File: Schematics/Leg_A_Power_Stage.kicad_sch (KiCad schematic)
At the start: 40 parts, among them Q2 C3M0025065K, Q3 C3M0025065K, U1 UCC21710QDWRQ1, U2 UCC21710QDWRQ1

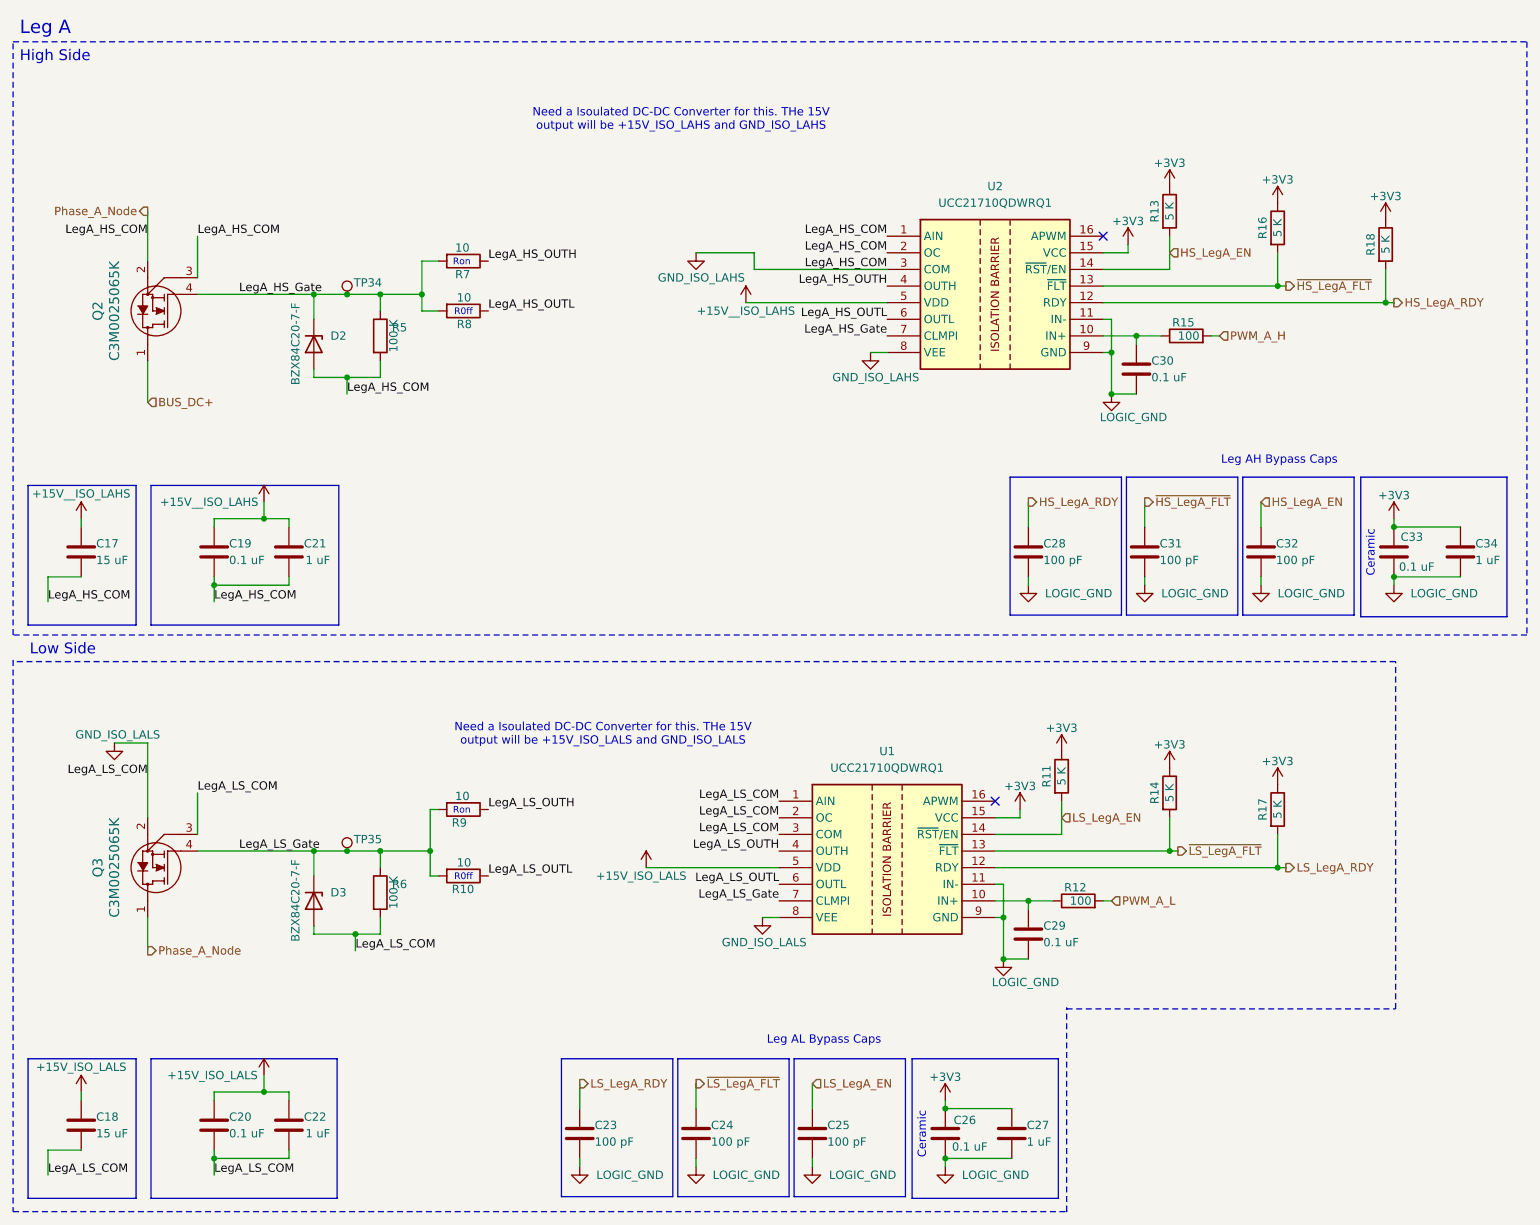
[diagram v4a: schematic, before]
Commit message: Fixing Full Bridge MOSFET ISO_GND to reference GND or DC-
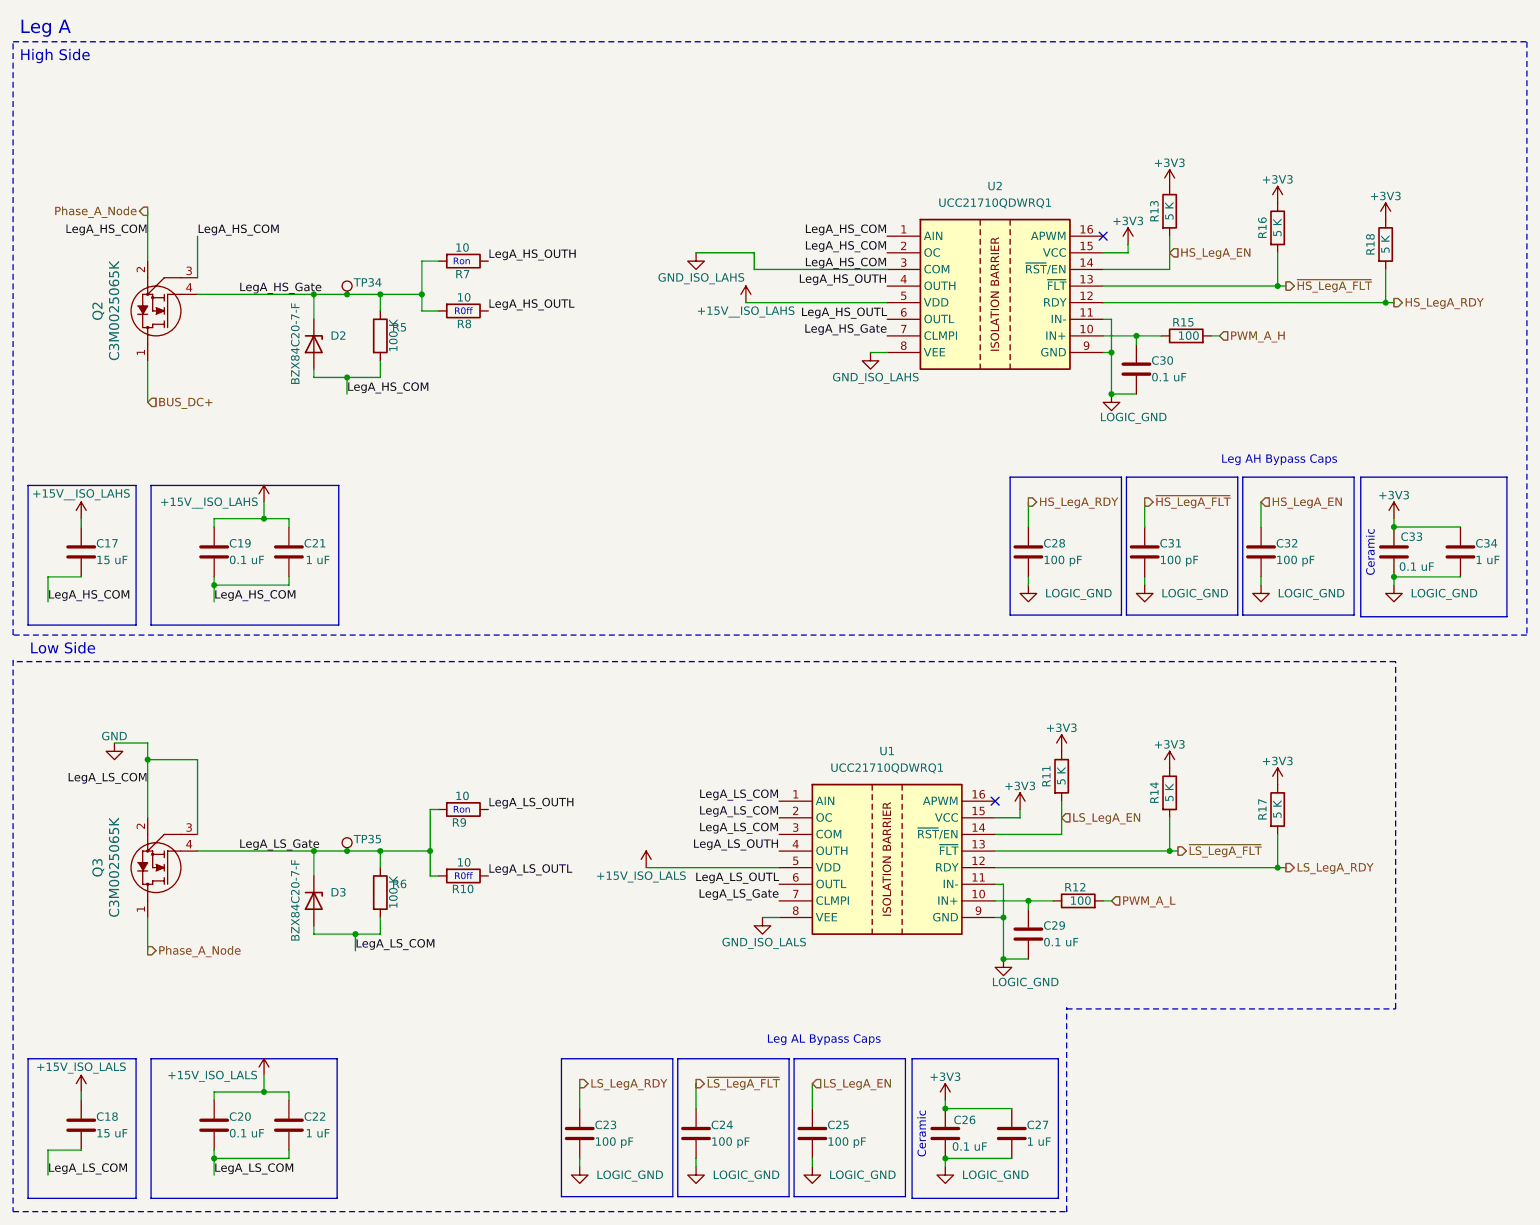
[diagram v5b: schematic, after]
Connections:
- net GND_ISO_LALS: no longer C18.2, C20.2, C22.2, D3.2 (A), Q3.2, Q3.3, R6.2, U1.1 (AIN), U1.2 (OC), U1.3 (COM)
- new net GND: C18.2, C20.2, C22.2, D3.2 (A), Q3.2, Q3.3, R6.2, U1.1 (AIN), U1.2 (OC), U1.3 (COM)
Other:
- note removed: "Need a Isoulated DC-DC Converter for this. THe 15V output will be +15V_ISO_LAHS and GND_ISO_LAHS"
- note removed: "Need a Isoulated DC-DC Converter for this. THe 15V output will be +15V_ISO_LALS and GND_ISO_LALS"
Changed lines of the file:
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@@
 		)
 	)
-	(text "Need a Isoulated DC-DC Converter for this. THe 15V\noutput will be +15V_ISO_LALS and GND_ISO_LALS"
-		(exclude_from_sim no)
-		(at 105.156 123.19 0)
-		(effects
-			(font
-				(size 1.27 1.27)
-			)
-		)
-	)
 	(text "Low Side\n"
 		(exclude_from_sim no)
@@
 		)
 	)
-	(text "Need a Isoulated DC-DC Converter for this. THe 15V\noutput will be +15V_ISO_LAHS and GND_ISO_LAHS"
-		(exclude_from_sim no)
-		(at 117.094 29.21 0)
-		(effects
-			(font
-				(size 1.27 1.27)
-			)
-		)
-	)
 	(text "Ceramic\n"
 		(exclude_from_sim no)
@@
 	)
 	(junction
+		(at 35.56 127)
+		(diameter 0)
+		(color 0 0 0 0)
+	)
+	(junction
 		(at 60.96 55.88)
 		(diameter 0)
@@
 	(wire
 		(pts
-			(xy 35.56 124.46) (xy 35.56 135.89)
+			(xy 168.91 134.62) (xy 168.91 135.89)
 		)
 		(stroke
@@
 	(wire
 		(pts
-			(xy 168.91 134.62) (xy 168.91 135.89)
+			(xy 45.72 187.96) (xy 45.72 190.5)
 		)
 		(stroke
@@
 	(wire
 		(pts
-			(xy 45.72 187.96) (xy 45.72 190.5)
+			(xy 119.38 187.96) (xy 119.38 189.23)
 		)
 		(stroke
@@
 	(wire
 		(pts
-			(xy 119.38 187.96) (xy 119.38 189.23)
+			(xy 170.18 148.59) (xy 173.99 148.59)
 		)
 		(stroke
@@
 	(wire
 		(pts
-			(xy 170.18 148.59) (xy 173.99 148.59)
+			(xy 208.28 138.43) (xy 208.28 143.51)
 		)
 		(stroke
@@
 	(wire
 		(pts
-			(xy 208.28 138.43) (xy 208.28 143.51)
+			(xy 43.18 127) (xy 35.56 127)
 		)
 		(stroke
@@
 	(wire
 		(pts
+			(xy 35.56 127) (xy 35.56 135.89)
+		)
+		(stroke
+			(width 0)
+			(type default)
+		)
+	)
+	(wire
+		(pts
 			(xy 71.12 140.97) (xy 71.12 143.51)
 		)
@@
 	(wire
 		(pts
-			(xy 43.18 132.08) (xy 43.18 138.43)
-		)
-		(stroke
-			(width 0)
-			(type default)
-		)
-	)
-	(wire
-		(pts
 			(xy 182.88 71.12) (xy 186.69 71.12)
 		)
@@
 	(wire
 		(pts
+			(xy 43.18 138.43) (xy 43.18 127)
+		)
+		(stroke
+			(width 0)
+			(type default)
+		)
+	)
+	(wire
+		(pts
 			(xy 45.72 99.06) (xy 45.72 100.33)
 		)
@@
 	(wire
 		(pts
+			(xy 35.56 124.46) (xy 35.56 127)
+		)
+		(stroke
+			(width 0)
+			(type default)
+		)
+	)
+	(wire
+		(pts
 			(xy 45.72 177.8) (xy 45.72 179.07)
 		)
@@
 		)
 	)
-	(label "LegA_LS_COM"
-		(at 43.18 132.08 0)
-		(effects
-			(font
-				(size 1.27 1.27)
-			)
-			(justify left bottom)
-		)
-	)
 	(label "LegA_HS_Gate"
 		(at 49.53 55.88 0)
@@
 	)
 	(label "LegA_LS_COM"
-		(at 35.56 129.54 180)
+		(at 35.56 130.81 180)
 		(effects
 			(font
@@
 	)
 	(symbol
+		(lib_id "power:GND")
+		(at 30.48 124.46 0)
+		(unit 1)
+		(body_style 1)
+		(exclude_from_sim no)
+		(in_bom yes)
+		(on_board yes)
+		(in_pos_files yes)
+		(dnp no)
+		(property "Reference" "#PWR023"
+			(at 30.48 130.81 0)
+			(hide yes)
+			(show_name no)
+			(do_not_autoplace no)
+			(effects
+				(font
+					(size 1.27 1.27)
+				)
+			)
+		)
+		(property "Value" "GND"
+			(at 30.48 123.444 0)
+			(show_name no)
+			(do_not_autoplace no)
+			(effects
+				(font
+					(size 1.27 1.27)
+				)
+			)
+		)
+		(property "Footprint" ""
+			(at 30.48 124.46 0)
+			(hide yes)
+			(show_name no)
+			(do_not_autoplace no)
+			(effects
+				(font
+					(size 1.27 1.27)
+				)
+			)
+		)
+		(property "Datasheet" ""
+			(at 30.48 124.46 0)
+			(hide yes)
+			(show_name no)
+			(do_not_autoplace no)
+			(effects
+				(font
+					(size 1.27 1.27)
+				)
+			)
+		)
+		(property "Description" "Power symbol creates a global label with name \"GND\" , ground"
+			(at 30.48 124.46 0)
+			(hide yes)
+			(show_name no)
+			(do_not_autoplace no)
+			(effects
+				(font
+					(size 1.27 1.27)
+				)
+			)
+		)
+		(pin "1"
+		)
+		(instances
+			(project "SiC_Single_Phase_Inverter"
+				(path "/a1ed0539-9735-4ad1-a8fd-87e26e7fce16/b6e78e1f-718a-4f31-892b-d9c389541b0d/df0e594b-c560-4977-9819-59c4a1d47101"
+					(reference "#PWR023")
+					(unit 1)
+				)
+			)
+		)
+	)
+	(symbol
 		(lib_id "SiC_Inverter:RT1206BRD075KL")
 		(at 224.79 48.26 0)
@@
 					(unit 1)
 				)
-			)
-		)
-	)
-	(symbol
-		(lib_id "power:GNDS")
-		(at 30.48 124.46 0)
-		(unit 1)
-		(body_style 1)
-		(exclude_from_sim no)
-		(in_bom yes)
-		(on_board yes)
-		(in_pos_files yes)
-		(dnp no)
-		(property "Reference" "#PWR023"
-			(at 30.48 130.81 0)
-			(hide yes)
-			(show_name no)
-			(do_not_autoplace no)
-			(effects
-				(font
-					(size 1.27 1.27)
-				)
-			)
-		)
-		(property "Value" "GND_ISO_LALS"
-			(at 30.988 123.19 0)
-			(show_name no)
-			(do_not_autoplace no)
-			(effects
-				(font
-					(size 1.27 1.27)
-				)
-			)
-		)
-		(property "Footprint" ""
-			(at 30.48 124.46 0)
-			(hide yes)
-			(show_name no)
-			(do_not_autoplace no)
-			(effects
-				(font
-					(size 1.27 1.27)
-				)
-			)
-		)
-		(property "Datasheet" ""
-			(at 30.48 124.46 0)
-			(hide yes)
-			(show_name no)
-			(do_not_autoplace no)
-			(effects
-				(font
-					(size 1.27 1.27)
-				)
-			)
-		)
-		(property "Description" "Power symbol creates a global label with name \"GNDS\" , signal ground"
-			(at 30.48 124.46 0)
-			(hide yes)
-			(show_name no)
-			(do_not_autoplace no)
-			(effects
-				(font
-					(size 1.27 1.27)
-				)
-			)
-		)
-		(pin "1"
-		)
-		(instances
-			(project "SiC_Single_Phase_Inverter"
-				(path "/a1ed0539-9735-4ad1-a8fd-87e26e7fce16/b6e78e1f-718a-4f31-892b-d9c389541b0d/df0e594b-c560-4977-9819-59c4a1d47101"
-					(reference "#PWR023")
-					(unit 1)
-				)
